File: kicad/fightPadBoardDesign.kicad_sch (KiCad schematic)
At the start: 30 parts

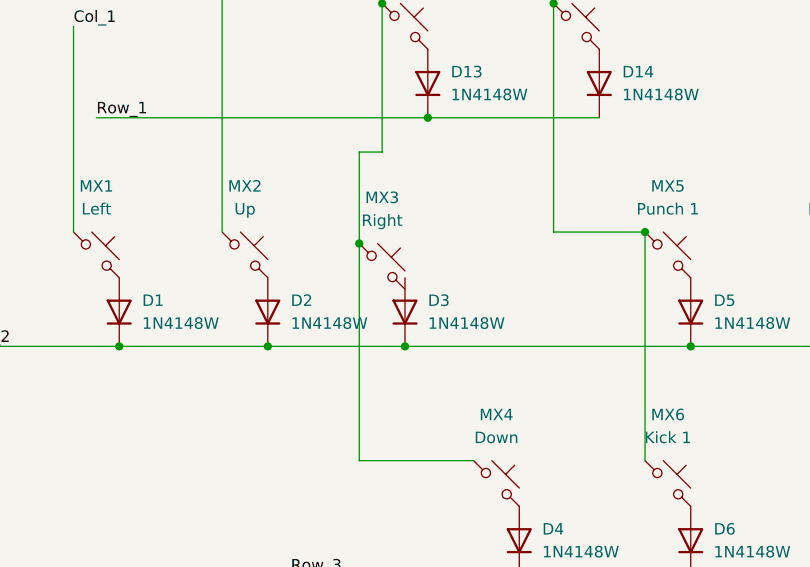
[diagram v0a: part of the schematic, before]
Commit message: Added layout and got the placement correct with housing
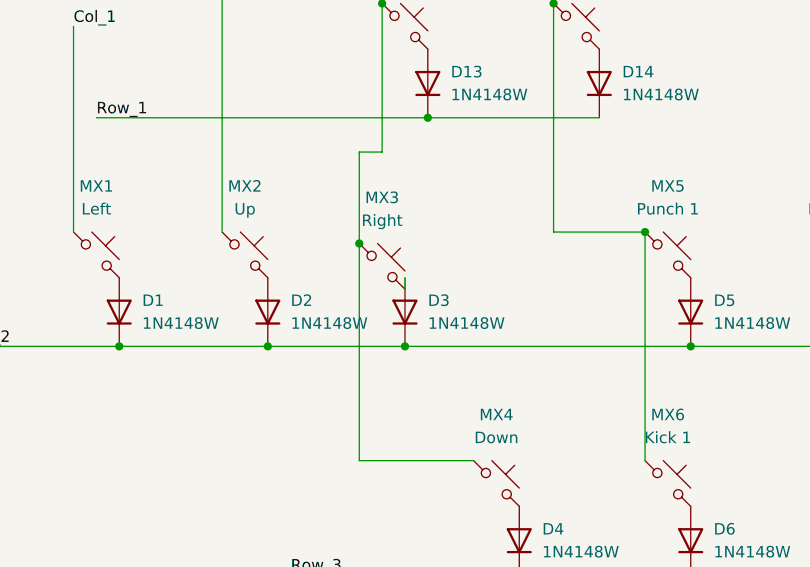
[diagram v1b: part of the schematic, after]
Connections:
- net at D3.2 (A): now also MX3.2
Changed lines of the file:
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@@
+	(wire
+		(pts
+			(xy 158.75 68.58) (xy 158.75 69.85)
+		)
+		(stroke
+			(width 0)
+			(type default)
+		)
+	)
 	(wire
 		(pts
